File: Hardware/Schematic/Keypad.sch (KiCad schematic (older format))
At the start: 8 parts, among them U1 TCA8418RTWR

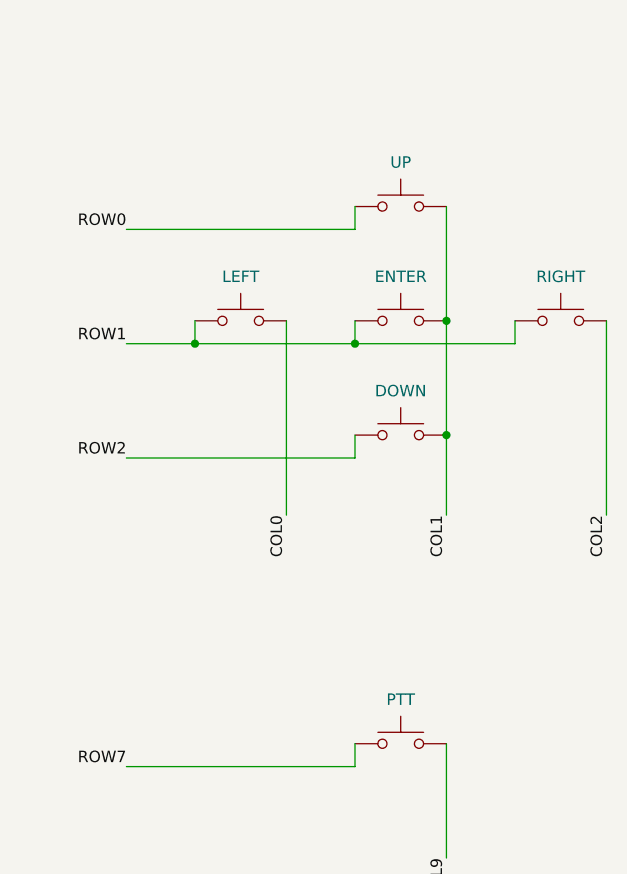
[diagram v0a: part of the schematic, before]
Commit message: Added E-INK display connector and datasheet
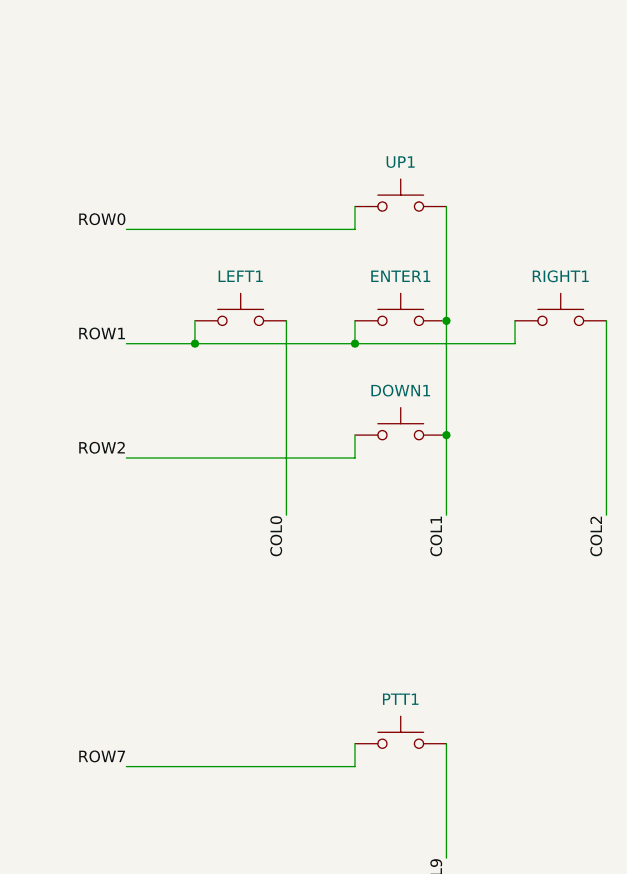
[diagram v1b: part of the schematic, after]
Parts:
- renumbered DOWN to DOWN1, ENTER to ENTER1, LEFT to LEFT1, PTT to PTT1, RIGHT to RIGHT1, UP to UP1
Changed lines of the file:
@@
 $Descr A4 11693 8268
 encoding utf-8
-Sheet 4 4
+Sheet 4 5
 Title ""
 Date ""
@@
 	2250 4100 2250 4400
 $Comp
-L Switch:SW_Push UP
+L Switch:SW_Push UP1
 U 1 1 5D17C122
 P 6450 2750
-F 0 "UP" H 6450 2943 50  0000 C CNN
+F 0 "UP1" H 6450 2943 50  0000 C CNN
 F 1 "SW_Push" H 6450 2944 50  0001 C CNN
 F 2 "Button_Switch_SMD:SW_SPST_B3S-1000" H 6450 2950 50  0001 C CNN
@@
 $EndComp
 $Comp
-L Switch:SW_Push ENTER
+L Switch:SW_Push ENTER1
 U 1 1 5D17D061
 P 6450 3250
-F 0 "ENTER" H 6450 3443 50  0000 C CNN
+F 0 "ENTER1" H 6450 3443 50  0000 C CNN
 F 1 "SW_Push" H 6450 3444 50  0001 C CNN
 F 2 "Button_Switch_SMD:SW_SPST_B3S-1000" H 6450 3450 50  0001 C CNN
@@
 $EndComp
 $Comp
-L Switch:SW_Push DOWN
+L Switch:SW_Push DOWN1
 U 1 1 5D17D8E5
 P 6450 3750
-F 0 "DOWN" H 6450 3943 50  0000 C CNN
+F 0 "DOWN1" H 6450 3943 50  0000 C CNN
 F 1 "SW_Push" H 6450 3944 50  0001 C CNN
 F 2 "Button_Switch_SMD:SW_SPST_B3S-1000" H 6450 3950 50  0001 C CNN
@@
 $EndComp
 $Comp
-L Switch:SW_Push RIGHT
+L Switch:SW_Push RIGHT1
 U 1 1 5D17DC10
 P 7150 3250
-F 0 "RIGHT" H 7150 3443 50  0000 C CNN
+F 0 "RIGHT1" H 7150 3443 50  0000 C CNN
 F 1 "SW_Push" H 7150 3444 50  0001 C CNN
 F 2 "Button_Switch_SMD:SW_SPST_B3S-1000" H 7150 3450 50  0001 C CNN
@@
 $EndComp
 $Comp
-L Switch:SW_Push LEFT
+L Switch:SW_Push LEFT1
 U 1 1 5D17D4DE
 P 5750 3250
-F 0 "LEFT" H 5750 3443 50  0000 C CNN
+F 0 "LEFT1" H 5750 3443 50  0000 C CNN
 F 1 "SW_Push" H 5750 3444 50  0001 C CNN
 F 2 "Button_Switch_SMD:SW_SPST_B3S-1000" H 5750 3450 50  0001 C CNN
@@
 	3900 2700 4000 2700
 $Comp
-L Switch:SW_Push PTT
+L Switch:SW_Push PTT1
 U 1 1 5D18E70F
 P 6450 5100
-F 0 "PTT" H 6450 5293 50  0000 C CNN
+F 0 "PTT1" H 6450 5293 50  0000 C CNN
 F 1 "SW_Push" H 6450 5294 50  0001 C CNN
 F 2 "Button_Switch_SMD:SW_SPST_B3S-1000" H 6450 5300 50  0001 C CNN

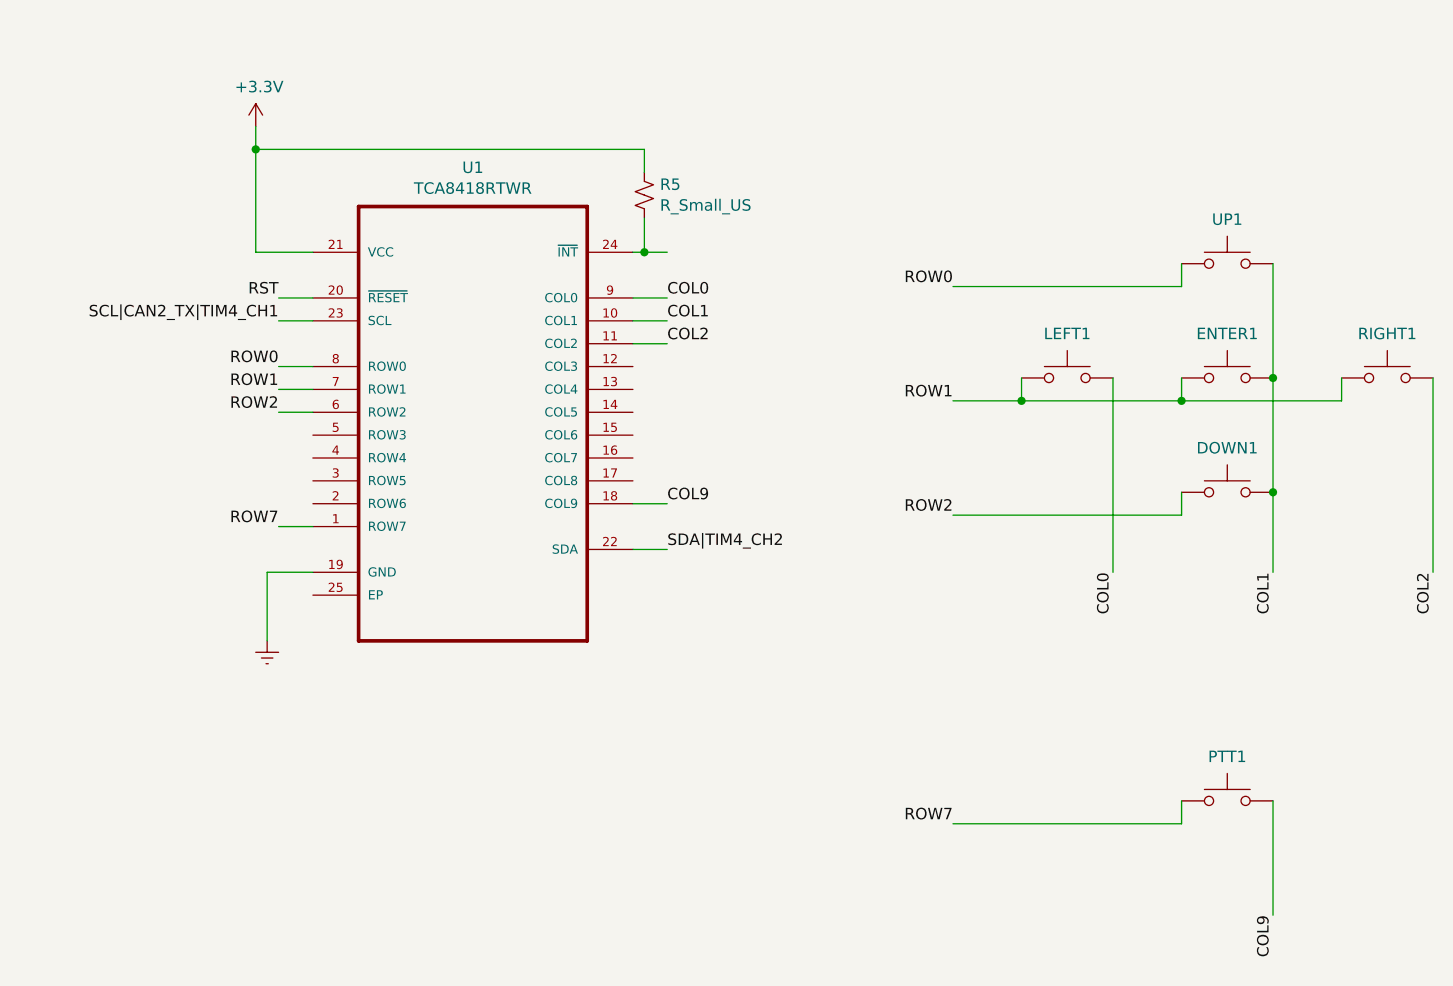
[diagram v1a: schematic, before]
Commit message: Lots of schematic updates
Lots of stuff...

* Added a new 8-pin TVS diode array
* Finalized the display connector
* Corrected the net labels to global labels so they span across sheets
* Added a 5V linear voltage regulator and LEDs to debug power
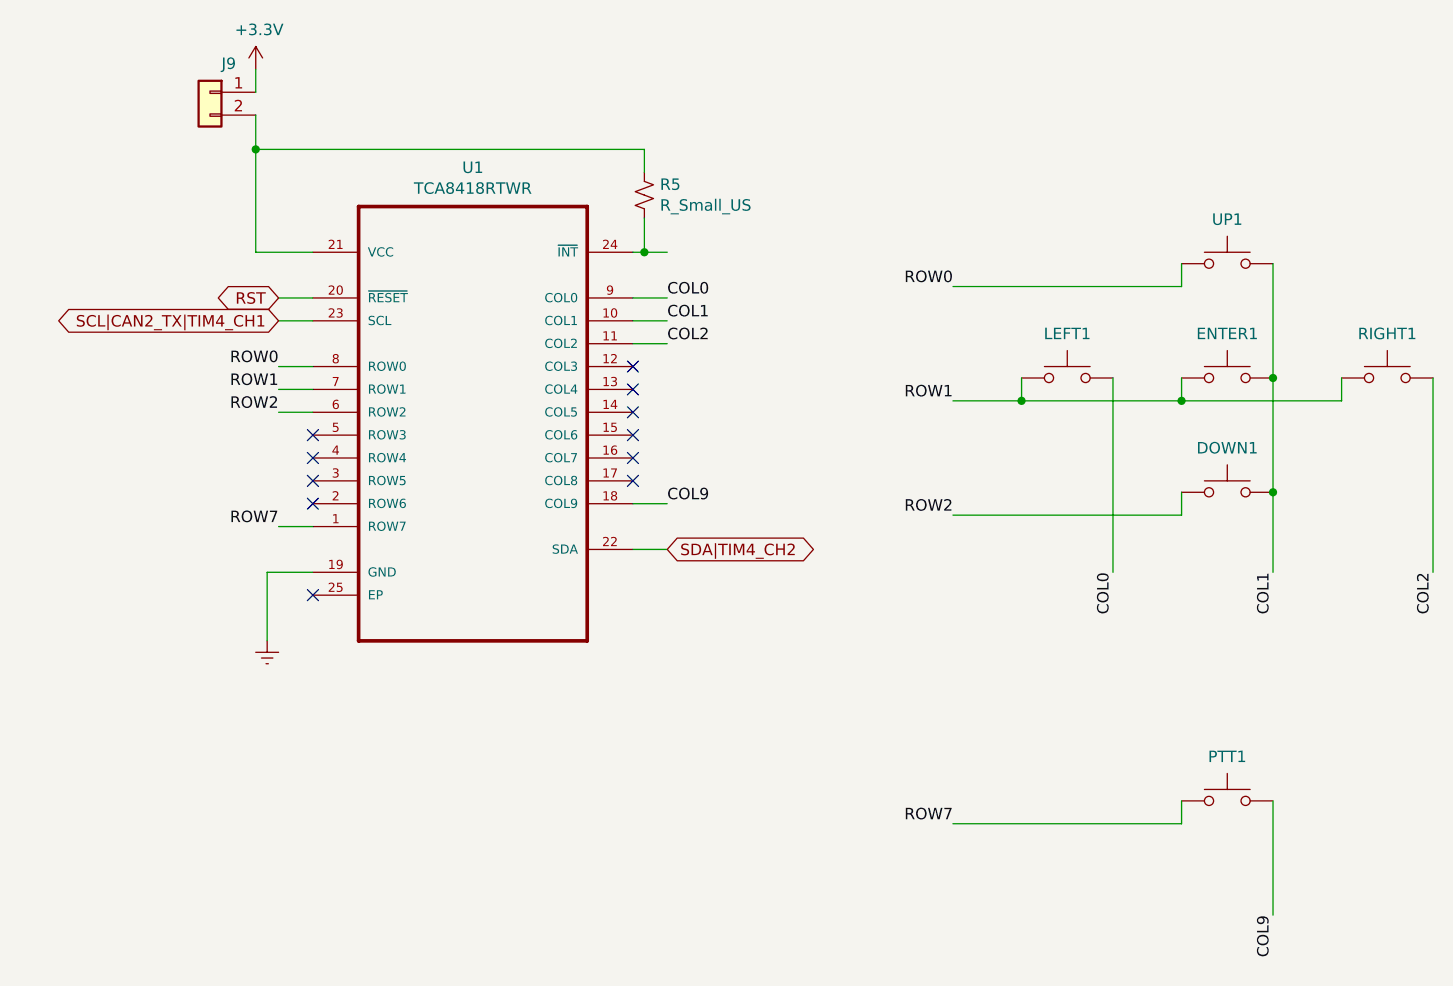
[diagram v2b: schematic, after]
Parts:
- added J9: Conn_01x02, Connector_PinHeader_2.54mm:PinHeader_1x02_P2.54mm_Vertical, symbol Connector_Generic:Conn_01x02
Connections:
- net +3V3: now also J9.1 (Pin_1); no longer R5.1, U1.21 (VCC)
- new net: J9.2 (Pin_2), R5.1, U1.21 (VCC)
- no-connect marks 0 -> 11
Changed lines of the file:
@@
 $Descr A4 11693 8268
 encoding utf-8
-Sheet 4 5
+Sheet 4 6
 Title ""
 Date ""
@@
 Comment4 ""
 $EndDescr
-$Comp
-L TCA8418RTWR:TCA8418RTWR U?
-U 1 1 5D178EB2
-P 3150 3300
-AR Path="/5D178EB2" Ref="U?"  Part="1"
-AR Path="/5D1772AD/5D178EB2" Ref="U1"  Part="1"
-F 0 "U1" H 3150 4270 50  0000 C CNN
-F 1 "TCA8418RTWR" H 3150 4179 50  0000 C CNN
-F 2 "QFN50P400X400X80-25N" H 3150 3300 50  0001 L BNN
-F 3 "" H 3150 3300 50  0001 L BNN
-F 4 "None" H 3150 3300 50  0001 L BNN "Field4"
-F 5 "Unavailable" H 3150 3300 50  0001 L BNN "Field5"
-F 6 "WQFN-24 Texas Instruments" H 3150 3300 50  0001 L BNN "Field6"
-F 7 "TCA8418RTWR" H 3150 3300 50  0001 L BNN "Field7"
-F 8 "I2C Controlled Keypad Scan IC 24-Pin WQFN EP T/R" H 3150 3300 50  0001 L BNN "Field8"
-	1    3150 3300
-	1    0    0    -1
-$EndComp
 Wire Wire Line
 	3850 4000 4000 4000
-Text Label 4000 4000 0    50   ~ 0
-SDA|TIM4_CH2
 Wire Wire Line
 	2450 3000 2300 3000
-Text Label 2300 3000 2    50   ~ 0
-SCL|CAN2_TX|TIM4_CH1
 $Comp
 L power:Earth #PWR0115
@@
 Wire Wire Line
 	3850 3100 4000 3100
-Wire Wire Line
-	2450 3200 2300 3200
 Wire Wire Line
 	2450 3300 2300 3300
@@
 Text Label 4000 3100 0    50   ~ 0
 COL2
-Text Label 2300 3200 2    50   ~ 0
-ROW0
-Text Label 2300 3300 2    50   ~ 0
-ROW1
 Text Label 2300 3400 2    50   ~ 0
 ROW2
@@
 L power:+3.3V #PWR0116
 U 1 1 5D186F12
-P 2200 2150
-F 0 "#PWR0116" H 2200 2000 50  0001 C CNN
-F 1 "+3.3V" H 2215 2323 50  0000 C CNN
-F 2 "" H 2200 2150 50  0001 C CNN
-F 3 "" H 2200 2150 50  0001 C CNN
-	1    2200 2150
+P 2200 1900
+F 0 "#PWR0116" H 2200 1750 50  0001 C CNN
+F 1 "+3.3V" H 2215 2073 50  0000 C CNN
+F 2 "" H 2200 1900 50  0001 C CNN
+F 3 "" H 2200 1900 50  0001 C CNN
+	1    2200 1900
 	1    0    0    -1
 $EndComp
 Wire Wire Line
 	2300 2900 2450 2900
-Text Label 2300 2900 2    50   ~ 0
-RST
 Wire Wire Line
 	3850 2700 3900 2700
 Wire Wire Line
-	2200 2150 2200 2250
+	2200 1900 2200 2000
 Wire Wire Line
 	2200 2250 3900 2250
-Connection ~ 2200 2250
 Wire Wire Line
 	2200 2250 2200 2700
@@
 Wire Wire Line
 	2300 3900 2450 3900
+NoConn ~ 2450 4200
+NoConn ~ 2450 3800
+NoConn ~ 2450 3700
+NoConn ~ 2450 3600
+NoConn ~ 2450 3500
+NoConn ~ 3850 3700
+NoConn ~ 3850 3600
+NoConn ~ 3850 3500
+NoConn ~ 3850 3400
+NoConn ~ 3850 3300
+NoConn ~ 3850 3200
+$Comp
+L Connector_Generic:Conn_01x02 J9
+U 1 1 5D205776
+P 2000 2000
+F 0 "J9" H 1918 2125 50  0000 C CNN
+F 1 "Conn_01x02" H 1918 2126 50  0001 C CNN
+F 2 "Connector_PinHeader_2.54mm:PinHeader_1x02_P2.54mm_Vertical" H 2000 2000 50  0001 C CNN
+F 3 "~" H 2000 2000 50  0001 C CNN
+	1    2000 2000
+	-1   0    0    -1
+$EndComp
+Wire Wire Line
+	2200 2250 2200 2100
+Connection ~ 2200 2250
+Text GLabel 4000 4000 2    50   BiDi ~ 0
+SDA|TIM4_CH2
+Text Label 2300 3300 2    50   ~ 0
+ROW1
+Text Label 2300 3200 2    50   ~ 0
+ROW0
+Wire Wire Line
+	2450 3200 2300 3200
+$Comp
+L TCA8418RTWR:TCA8418RTWR U?
+U 1 1 5D178EB2
+P 3150 3300
+AR Path="/5D178EB2" Ref="U?"  Part="1"
+AR Path="/5D1772AD/5D178EB2" Ref="U1"  Part="1"
+F 0 "U1" H 3150 4270 50  0000 C CNN
+F 1 "TCA8418RTWR" H 3150 4179 50  0000 C CNN
+F 2 "QFN50P400X400X80-25N" H 3150 3300 50  0001 L BNN
+F 3 "" H 3150 3300 50  0001 L BNN
+F 4 "None" H 3150 3300 50  0001 L BNN "Field4"
+F 5 "Unavailable" H 3150 3300 50  0001 L BNN "Field5"
+F 6 "WQFN-24 Texas Instruments" H 3150 3300 50  0001 L BNN "Field6"
+F 7 "TCA8418RTWR" H 3150 3300 50  0001 L BNN "Field7"
+F 8 "I2C Controlled Keypad Scan IC 24-Pin WQFN EP T/R" H 3150 3300 50  0001 L BNN "Field8"
+	1    3150 3300
+	1    0    0    -1
+$EndComp
+Text GLabel 2300 3000 0    50   BiDi ~ 0
+SCL|CAN2_TX|TIM4_CH1
+Text GLabel 2300 2900 0    50   BiDi ~ 0
+RST
 $EndSCHEMATC
